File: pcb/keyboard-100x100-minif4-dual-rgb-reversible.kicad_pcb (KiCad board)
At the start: 2 copper layers, 100 x 100 mm, 84 parts, among them J1 TRRS, U1 MiniF4, U2 SN74LVC1T45DBV

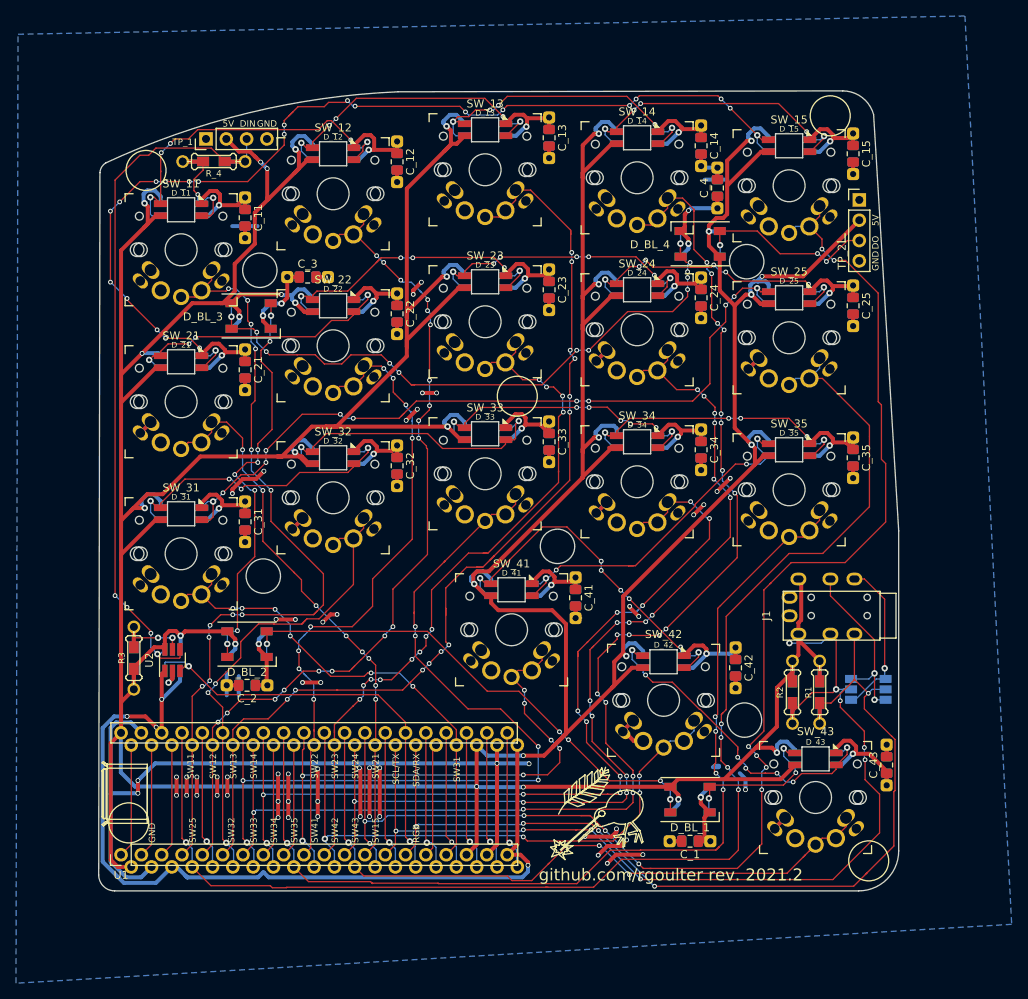
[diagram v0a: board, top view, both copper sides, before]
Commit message: Kicad: improve consistency of naming in schematic, PCB
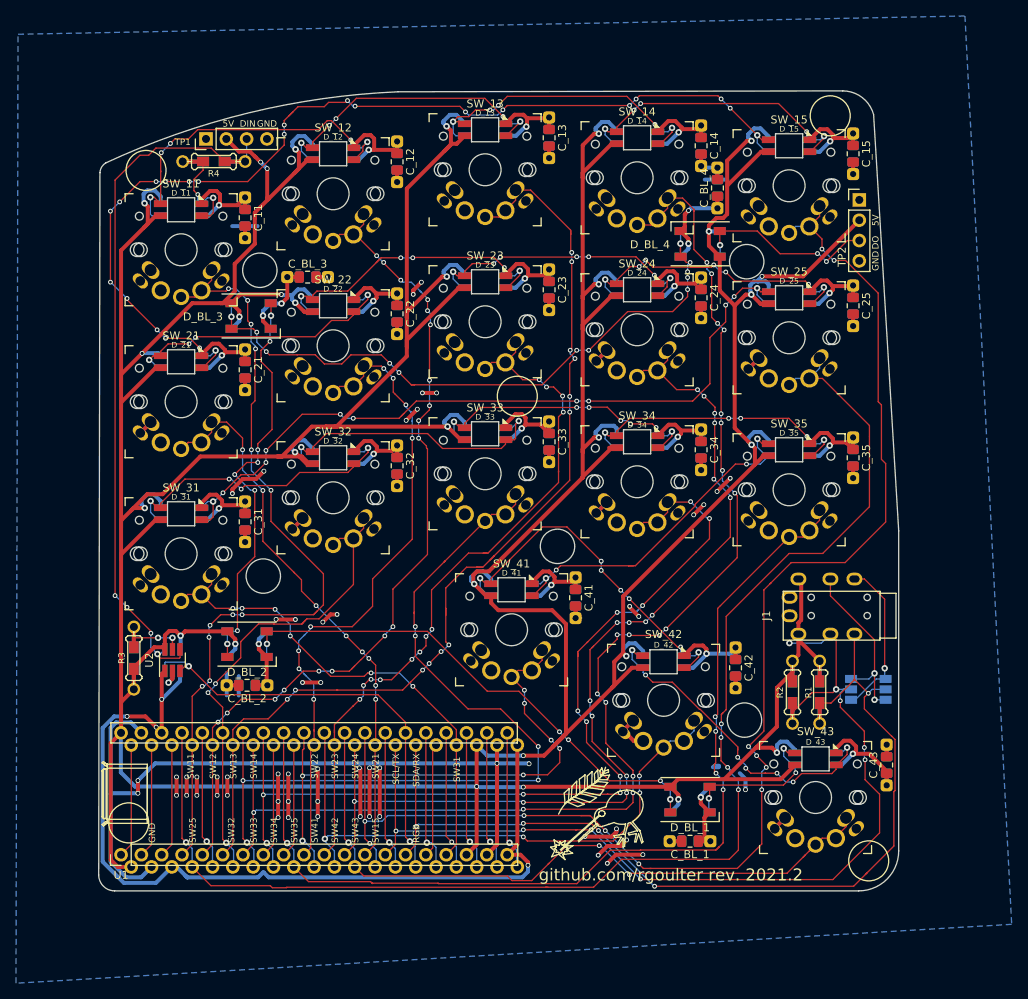
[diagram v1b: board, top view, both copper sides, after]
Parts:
- renumbered C_1 to C_BL_1, C_2 to C_BL_2, C_3 to C_BL_3, C_4 to C_BL_4, J_2 to J2, JP_1 to JP1, JP_2 to JP2, R_4 to R4, TP_1 to TP1, TP_2 to TP2

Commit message: Kicad: trace all the components together
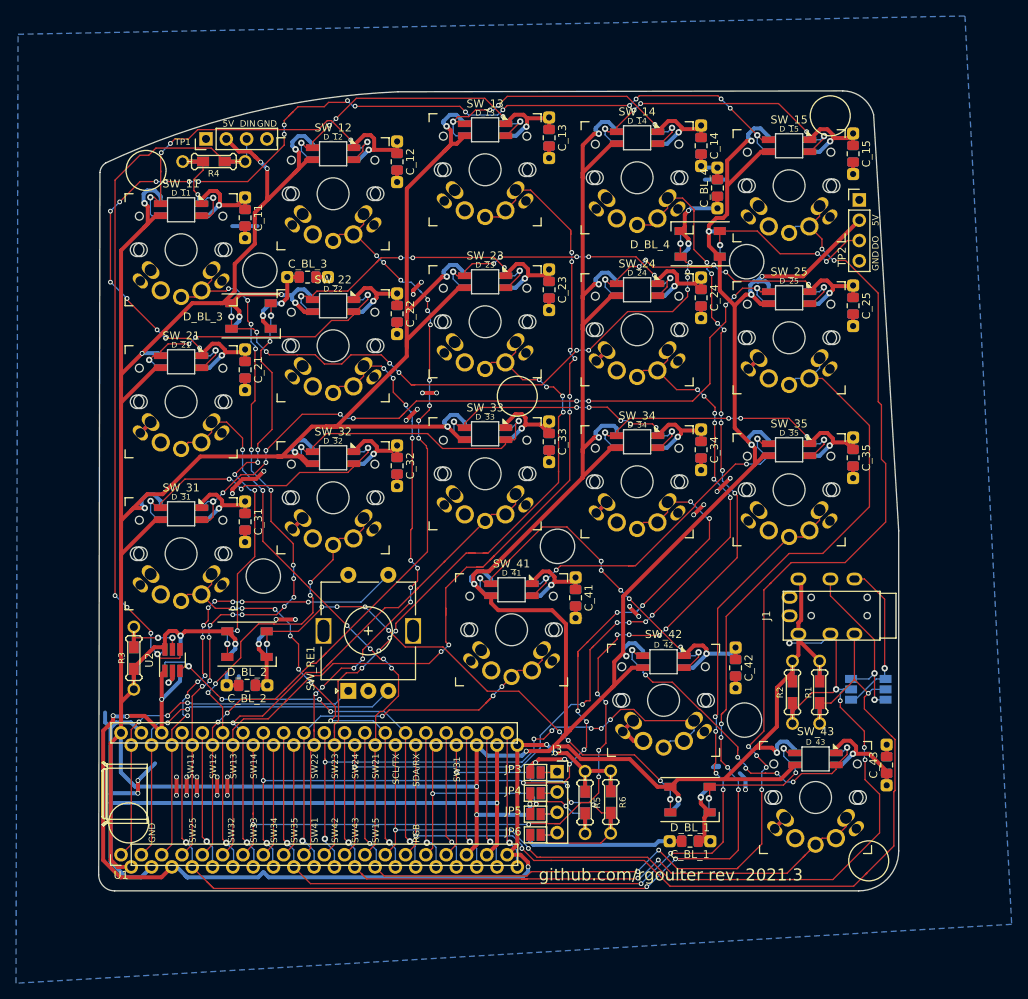
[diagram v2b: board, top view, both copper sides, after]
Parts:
- added J3: Conn_01x04_Female, Connector_PinSocket_2.54mm:PinSocket_1x04_P2.54mm_Vertical, F.Cu at (157.3, 135.1)
- added JP10: SolderJumper_2_Open, Jumper:SolderJumper-2_P1.3mm_Open_Pad1.0x1.5mm, B.Cu at (154.6, 135.2)
- added JP3: SolderJumper_2_Open, Jumper:SolderJumper-2_P1.3mm_Open_Pad1.0x1.5mm, F.Cu at (154.6, 135.2)
- added JP4: SolderJumper_2_Open, Jumper:SolderJumper-2_P1.3mm_Open_Pad1.0x1.5mm, F.Cu at (154.6, 137.8)
- added JP5: SolderJumper_2_Open, Jumper:SolderJumper-2_P1.3mm_Open_Pad1.0x1.5mm, F.Cu at (154.6, 140.4)
- added JP6: SolderJumper_2_Open, Jumper:SolderJumper-2_P1.3mm_Open_Pad1.0x1.5mm, F.Cu at (154.6, 143.0)
- added JP7: SolderJumper_2_Open, Jumper:SolderJumper-2_P1.3mm_Open_Pad1.0x1.5mm, B.Cu at (154.6, 143.0)
- added JP8: SolderJumper_2_Open, Jumper:SolderJumper-2_P1.3mm_Open_Pad1.0x1.5mm, B.Cu at (154.6, 140.4)
- added JP9: SolderJumper_2_Open, Jumper:SolderJumper-2_P1.3mm_Open_Pad1.0x1.5mm, B.Cu at (154.6, 137.8)
- added R5: 2.2k - 10k, ProjectLocal:Resistor-Hybrid, F.Cu at (160.8, 138.9)
- added R6: 2.2k - 10k, ProjectLocal:Resistor-Hybrid, F.Cu at (164.0, 138.9)
- added SW_RE1: Rotary_Encoder_Switch, Rotary_Encoder:RotaryEncoder_Alps_EC11E-Switch_Vertical_H20mm, F.Cu at (131.2, 125.0)
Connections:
- U1 pad 11: Net-(U1-Pad11) -> /SW31
- U1 pad 25: Net-(U1-Pad25) -> /RE_A
- U1 pad 26: Net-(U1-Pad26) -> /RE_B
- U1 pad 27: Net-(U1-Pad27) -> /SW_RE
- U1 pad 45: Net-(U1-Pad45) -> /OLED_SCL
- U1 pad 46: /SW31 -> /OLED_SDA
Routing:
- net /SW_RE: track 0.00 -> 58.8 mm, vias 0 -> 11
- net /OLED_SDA: track 0.00 -> 48.6 mm, vias 0 -> 4
- net /RE_B: track 0.00 -> 47.8 mm, vias 0 -> 2
- net /RE_A: track 0.00 -> 45.4 mm, vias 0 -> 3
- net /SW33: track 106.2 -> 69.5 mm, vias 6 -> 2
- net /OLED_SCL: track 0.00 -> 36.6 mm, vias 0 -> 3
- net /GND: track 221.2 -> 193.6 mm, vias 57 -> 33
- net Net-(U1-Pad11): track 17.3 -> 0.00 mm, vias 1 -> 0
- net /SW41: track 69.5 -> 53.2 mm, vias 7 -> 4
- net /SW24: track 125.0 -> 110.4 mm, vias 16 -> 12
- net Net-(U1-Pad27): track 14.2 -> 0.00 mm
- net Net-(U1-Pad25): track 14.2 -> 0.00 mm
- net Net-(U1-Pad45): track 14.2 -> 0.00 mm
- net Net-(U1-Pad26): track 14.2 -> 0.00 mm
- net /3V3: track 113.7 -> 126.3 mm, vias 4 -> 6
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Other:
- board text added: "github.com/rgoulter rev. 2021.3"
- board text removed: "github.com/rgoulter rev. 2021.2"

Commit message: Kicad: tidy some traces, update silkscreen labels of underside
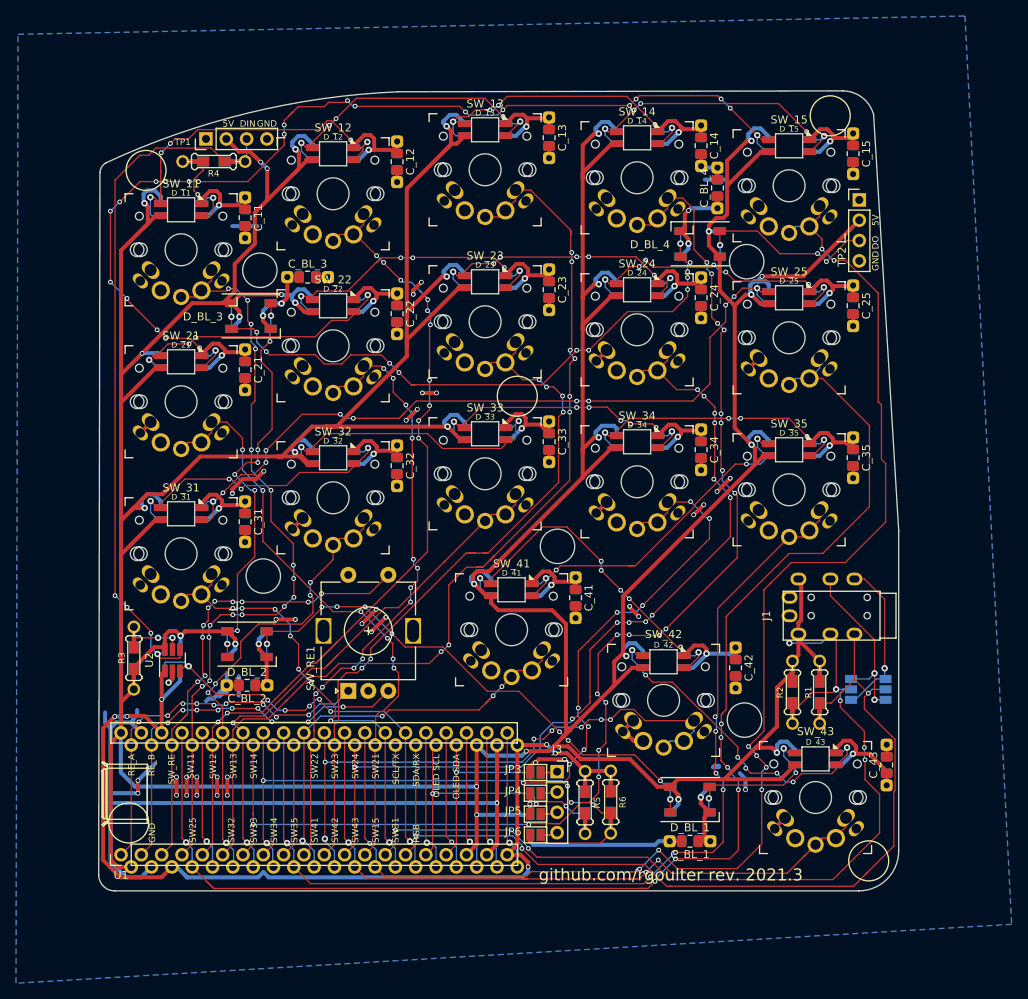
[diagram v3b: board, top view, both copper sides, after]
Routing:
- net /GND: track 193.6 -> 208.1 mm, vias 33 -> 37
- net /SW12: track 105.2 -> 109.0 mm
- net /SW21: track 73.2 -> 76.2 mm
- net /SW33: track 69.5 -> 71.4 mm
- net /RE_A: track 45.4 -> 47.1 mm, vias 3 -> 9
- net /RE_B: track 47.8 -> 49.3 mm, vias 2 -> 9
- net /3V3: track 126.3 -> 127.7 mm
- net /SW13: track 125.8 -> 124.6 mm
- net /SW43: track 87.3 -> 88.4 mm
- net /RGB_DIN_3V3: track 54.2 -> 55.2 mm, vias 5 -> 7
- net /SW25: track 170.7 -> 171.5 mm
- net /SW_RE: track 58.8 -> 58.4 mm, vias 11 -> 10
- net /SW23: track 88.9 -> 89.1 mm, vias 8 -> 6
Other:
- board text added: "OLED SCL"
- board text added: "OLED SDA"
- board text added: "RE_A"
- board text added: "RE_B"
- board text added: "SW_RE"
